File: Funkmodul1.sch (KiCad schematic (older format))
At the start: 48 parts, among them Q1 SSM3J334RLFTR-ND, Q2 AO3414, U1 MC74HC4538A, U2 MAX892, U3 ATMEGA128-16AU, Y1 Crystal_GND24

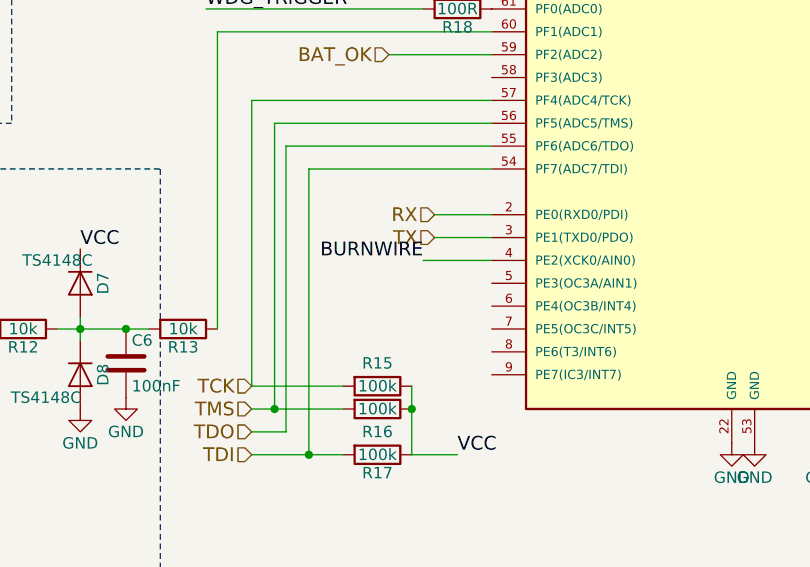
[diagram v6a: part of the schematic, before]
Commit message: Integrates Connectors in Design
Beginn to add mounting holes
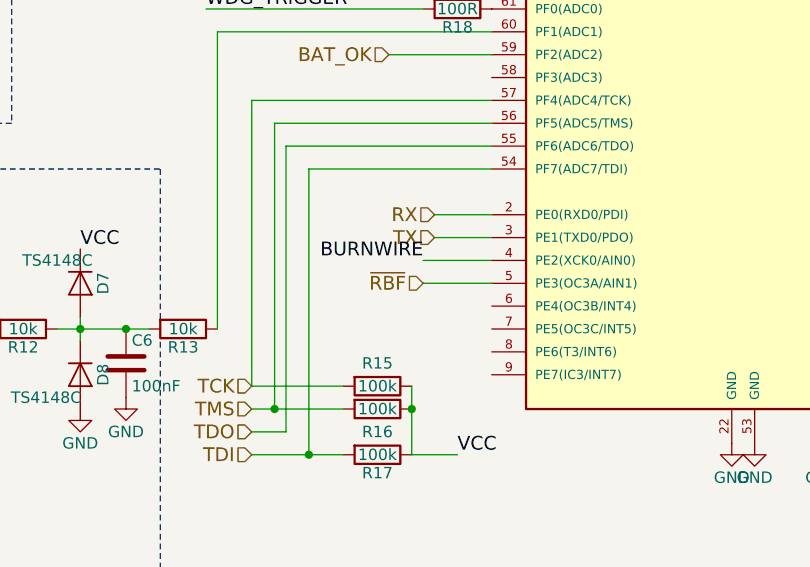
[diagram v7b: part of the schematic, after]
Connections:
- net ~RBF~: now reaches U3.5 (PE3(OC3A/AIN1))
